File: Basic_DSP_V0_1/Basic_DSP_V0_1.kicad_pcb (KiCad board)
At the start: 6 copper layers, 60 x 100 mm, 165 parts, among them J1 53048-0310, J10 53048-0310, J11 53048-0410, J12 Conn_ARM_SWD_TagConnect_TC2030, J14 53048-0210, J15 53048-0210, J16 Conn_02x08_Odd_Even, J2 53048-0310, J3 53048-0310, J4 USB_C_Receptacle_USB2.0_16P, J6 53048-0410, J7 53048-0310, J8 53048-0310, J9 53048-0310, Q1 AO3400A, Q2 AO3400A, Q3 AO3400A, U1 STM32F415RGTx, U10 TLV9161IDBVR, U2 CS4270, U3 TLV76733QWDRBRQ1, U5 NCP718BSN500T1G, U6 TLV9161IDBVR, U7 TLV9161IDBVR, U8 TLV9161IDBVR, U9 TLV9161IDBVR, Y1 ABM8G-24.000MHZ-18-D2Y-T3

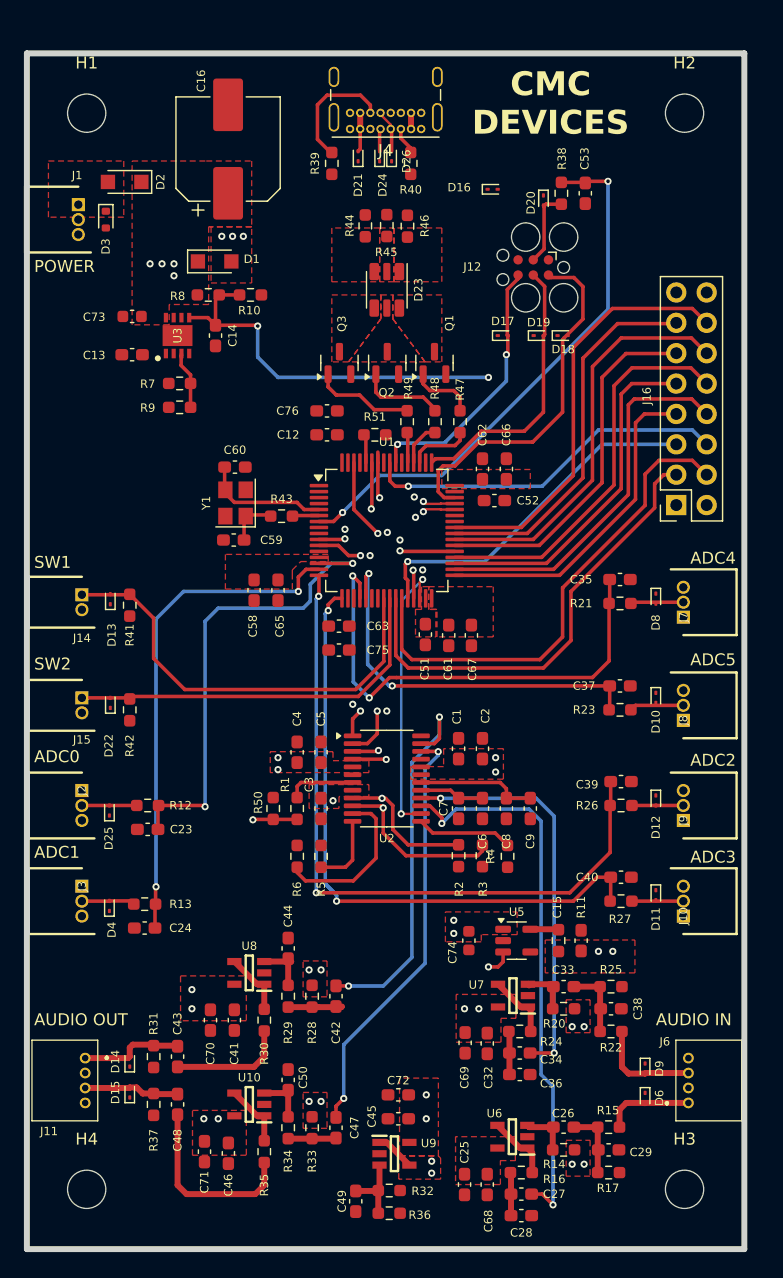
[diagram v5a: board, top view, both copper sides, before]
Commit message: All nets connected - DRC issues to be resolved
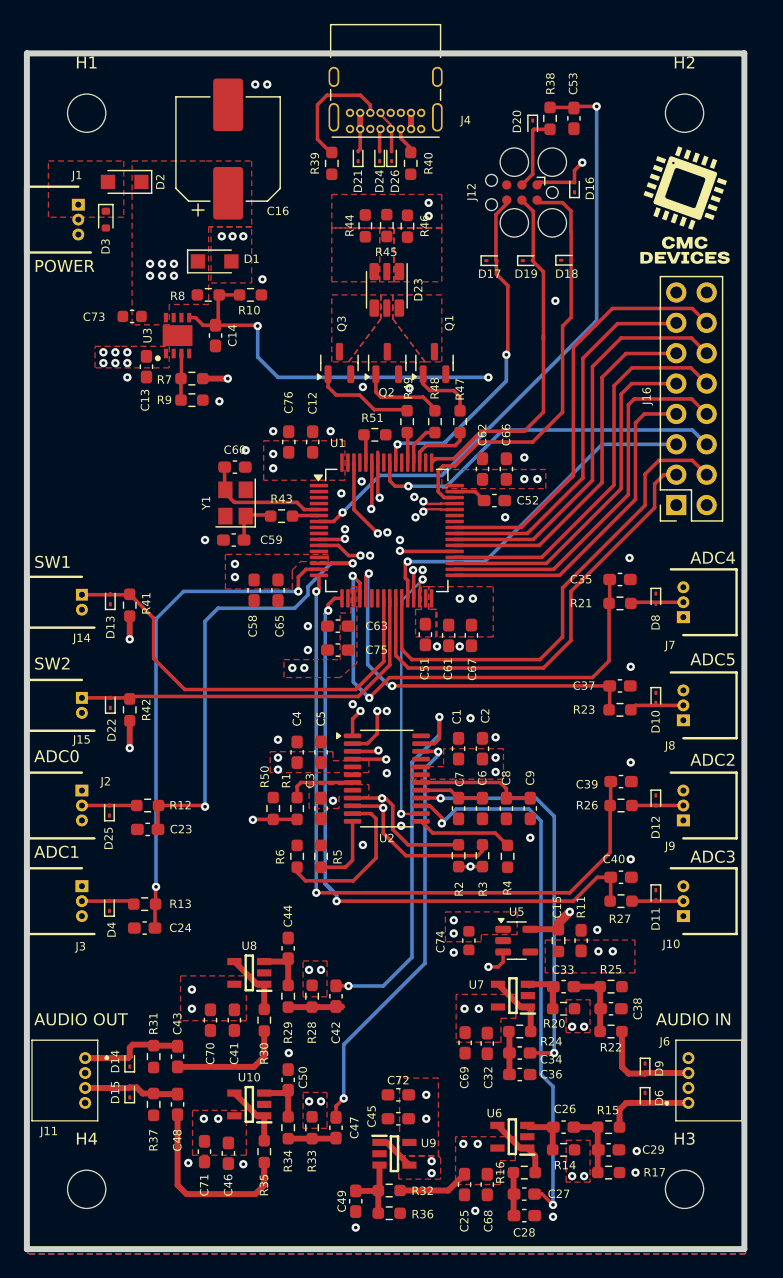
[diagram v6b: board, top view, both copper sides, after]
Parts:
- moved D16 6.85 mm to (119.2, 315.3), turned to 90 degrees
- moved D17 6.34 mm to (112.2, 321.4)
- moved J12 6.34 mm to (114.8, 315.7)
- moved C53 6.34 mm to (119.2, 309.5)
- moved R38 6.34 mm to (117.2, 309.5)
- moved D19 6.33 mm to (115.3, 321.4)
- moved D20 6.33 mm to (115.7, 310.1)
- moved D18 6.31 mm to (118.5, 321.4)
- moved C76 4.12 mm to (95.3, 336.6), turned to 90 degrees
- moved C13 1.56 mm to (83.4, 330.3), turned to -90 degrees
- moved C12 1.34 mm to (97.3, 336.6), turned to 90 degrees
- moved R9 1.19 mm to (87.2, 333.1), turned to 0 degrees
- moved R7 1.10 mm to (87.2, 331.3), turned to 180 degrees
- moved C27 0.25 mm to (115.0, 399.5)
- moved C28 0.25 mm to (115.0, 401.3)
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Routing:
- net +5V: track 2.38 -> 77.1 mm, vias 0 -> 3
- net +3V3: track 0.11 -> 13.6 mm, vias 3 -> 24
- net /Processor/SWCLK: track 23.0 -> 29.8 mm
- net /Processor/SWO: track 22.2 -> 28.5 mm
- net +5VA: track 0.00 -> 5.95 mm, vias 12 -> 14
- net /Processor/MCU_~{RST}: track 46.2 -> 51.8 mm
- net /Processor/SWDIO: track 30.2 -> 35.8 mm
- net Net-(U1-VCAP_2): track 0.00 -> 2.77 mm
- net Net-(U3-SNS): track 4.84 -> 4.13 mm
- net Net-(C27-Pad1): track 3.22 -> 3.72 mm
- net Net-(D1-K): vias 6 -> 8
- net GND: vias 9 -> 50
- added copper zone on In3.Cu, net +3V3
- added copper zone on F.Cu, net +5V
- added copper zone on B.Cu, net GND
- added copper zone on F.Cu, net GND
- added copper zone on In1.Cu, net GND
- added copper zone on In2.Cu, net GND
- added copper zone on In4.Cu, net GND
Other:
- board text added: "{ "ViaStitching": "0.2", "stitch_zone_0": { "HSpacing": "2", "VSpacing": "2", "Clearance": "0", "Randomize": false } }"
- board text removed: "CMC DEVICES"

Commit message: No errors from DRC on layout
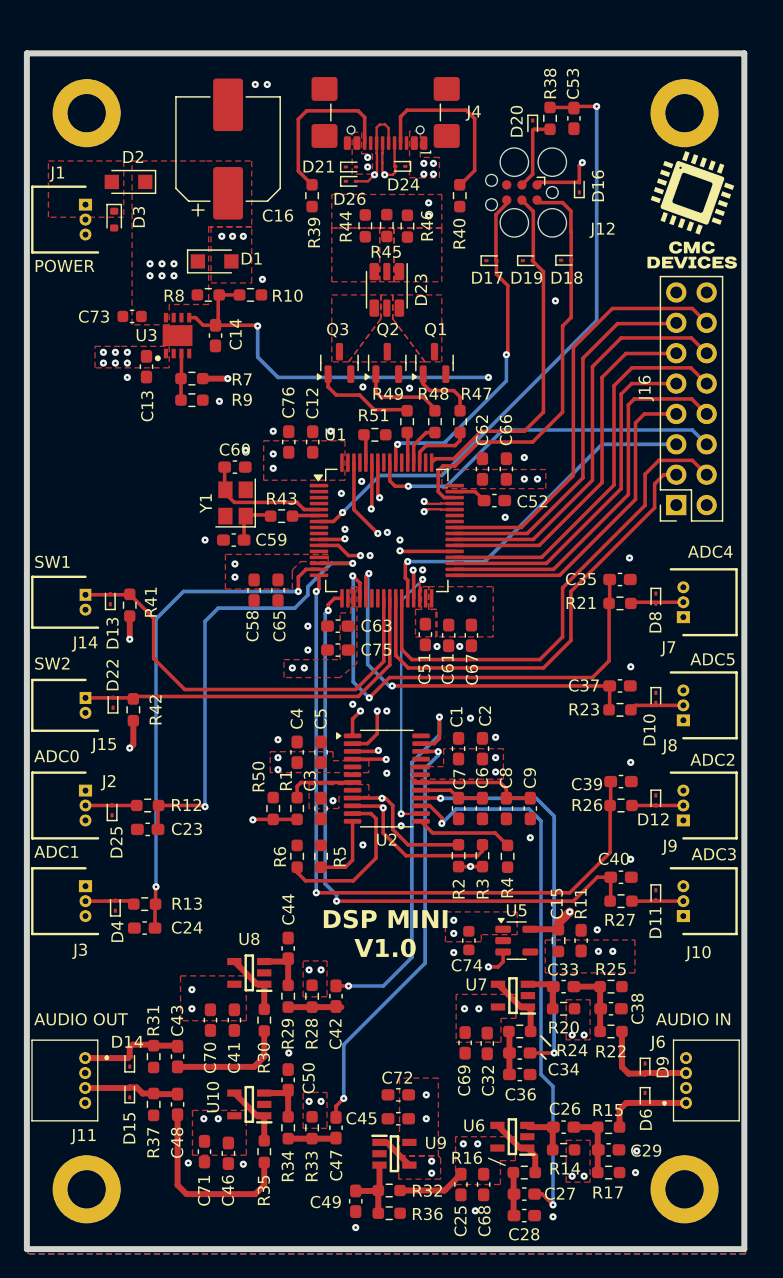
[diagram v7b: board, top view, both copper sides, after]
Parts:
- H1, H2, H3, H4: footprint MountingHole:MountingHole_3.2mm_M3 -> MountingHole:MountingHole_3.2mm_M3_ISO7380_Pad
- J4: footprint Connector_USB:USB_C_Receptacle_GCT_USB4085 -> Connector_USB:USB_C_Receptacle_GCT_USB4110
- moved R40 4.91 mm to (109.6, 316.0)
- moved D26 4.00 mm to (100.5, 314.8), turned to 0 degrees
- moved J4 3.90 mm to (103.4, 307.9)
- moved R39 3.16 mm to (97.2, 316.0)
- moved D24 1.93 mm to (104.6, 313.6), turned to 180 degrees
- moved D21 1.08 mm to (100.5, 313.6), turned to 0 degrees
- moved D3 0.70 mm to (80.7, 318.0)
- moved J1 0.60 mm to (78.3, 316.8)
- moved D4 0.50 mm to (80.8, 375.4)
- moved D16 0.40 mm to (119.6, 315.3)
- moved D2 0.33 mm to (81.9, 314.9)
- moved C68 0.30 mm to (111.6, 398.7)
- moved C25 0.30 mm to (109.7, 398.7)
- moved J14 0.30 mm to (78.3, 349.4)
- moved J15 0.30 mm to (78.3, 358.0)
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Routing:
- net Net-(J4-CC1): track 2.45 -> 15.0 mm
- net VBUS: track 4.63 -> 0.17 mm, vias 3 -> 9
- net Net-(J4-CC2): track 10.3 -> 14.2 mm
- net /Connections/USB_D+: track 40.1 -> 43.2 mm, vias 1 -> 2
- net /Connections/ADC_IN3: track 53.5 -> 52.4 mm
- net /Connections/USB_D-: track 40.9 -> 41.9 mm, vias 1 -> 2
- net /CODEC/I2C1_SCL: track 48.1 -> 47.2 mm
- net GND: vias 50 -> 48
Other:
- board text added: "DSP MINI V1.0"

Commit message: Tidy layout ready for review
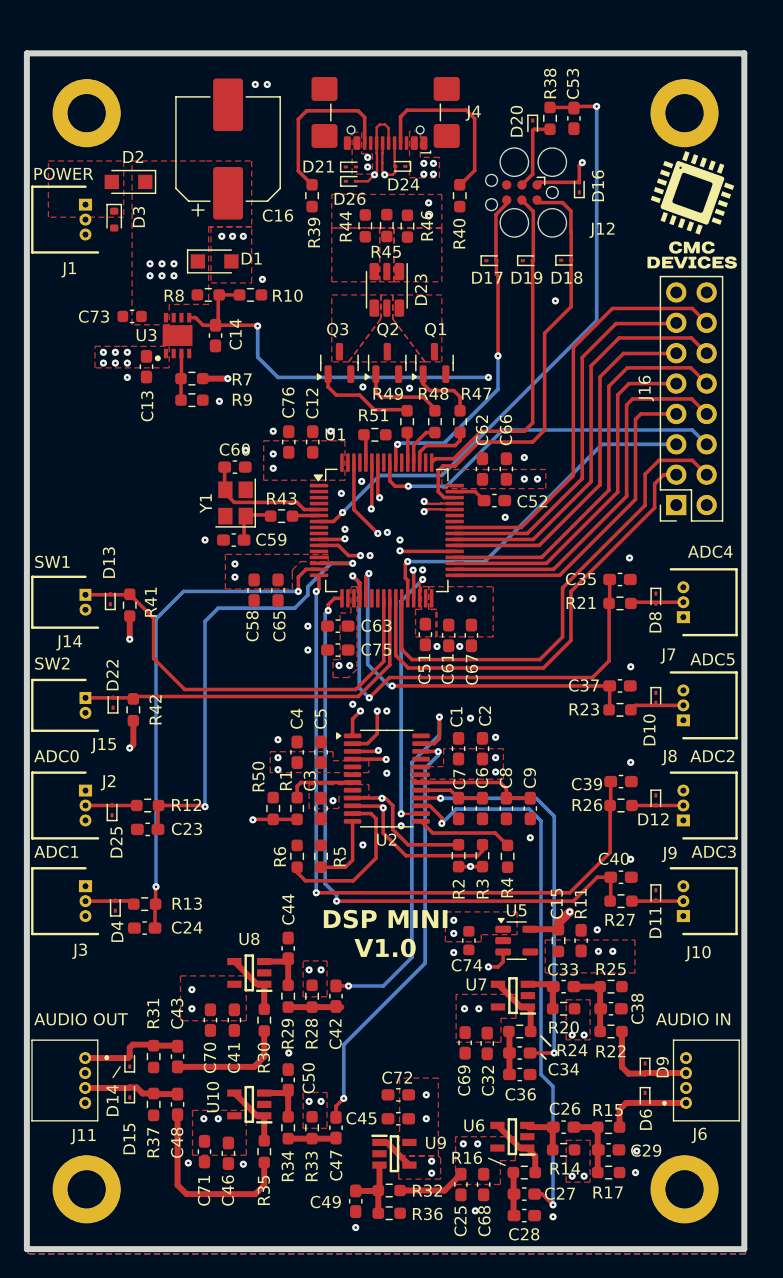
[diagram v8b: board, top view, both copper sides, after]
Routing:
- net /CODEC/I2C1_SCL: track 47.2 -> 48.3 mm
- net /CODEC/I2C1_SDA: track 42.1 -> 43.0 mm
- net /Processor/SWCLK: track 29.5 -> 28.8 mm
- net /Processor/SWO: track 28.5 -> 27.9 mm
